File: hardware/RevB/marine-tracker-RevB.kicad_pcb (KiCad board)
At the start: 2 copper layers, 65 x 58 mm, 108 parts, among them J1 USB-C, J2 BATTERY, J3 LTE_U.FL, J4 GNSS_L1_L5_U.FL, J5 Nano_SIM, Q1 AO3401A_REVERSE_POLARITY, Q2 MMBT2222A, U1 A7670G-LABE, U10 TPS3808G09DBVR, U11 TPL5111DDCR, U12 SN74LVC2G08DCUR, U13 SN74LVC1G14DBVR, U2 LC29H-AA, U3 BQ24074RGTR, U4 TPS7A2033PDBV, U5 TXS0104EPW, U6 W25Q32JWSSIM, U7 TPS22917DBV_GNSS_LOAD, U8 TPL5010_10MIN_WATCHDOG, U9 TPS3839K33DBZR

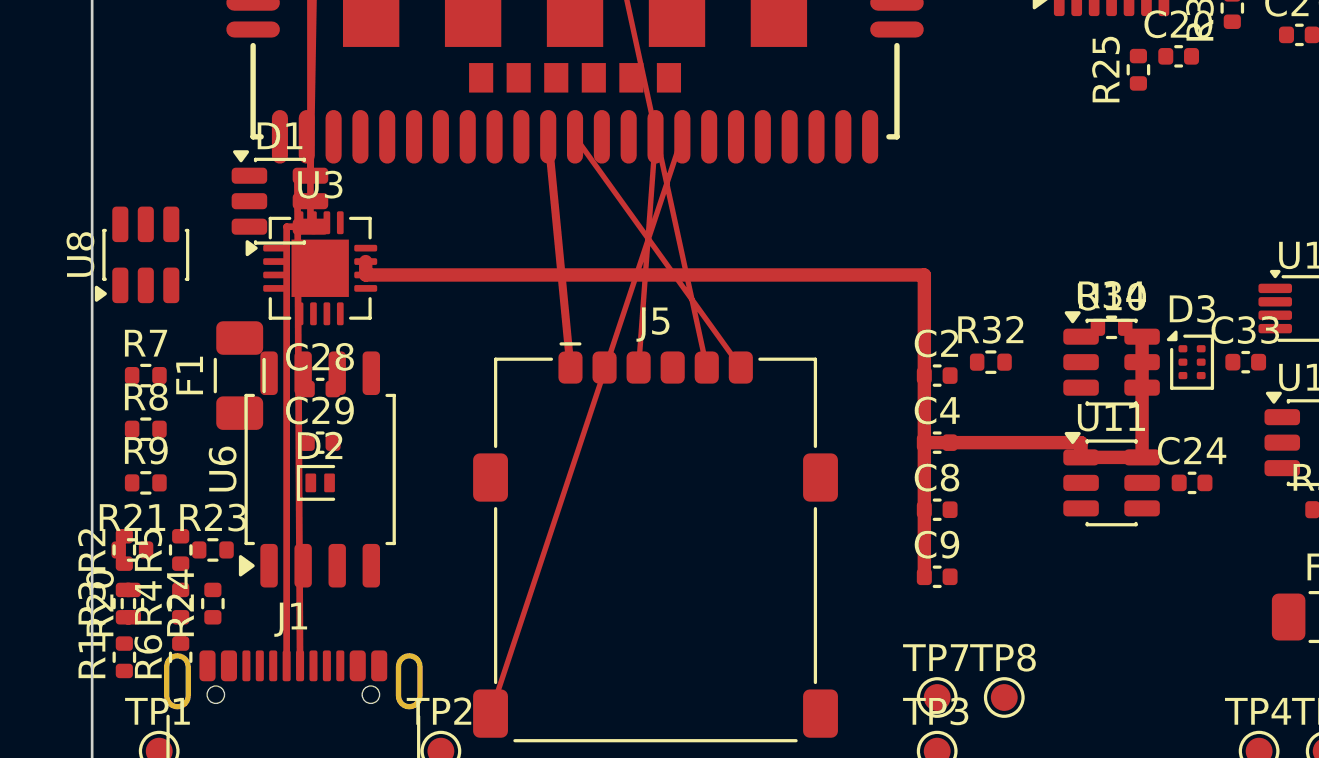
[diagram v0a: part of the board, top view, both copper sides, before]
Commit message: checkpoint: preserve RevB recovery routing state
Preserves the current validated RevB engineering checkpoint: WDT_DELAY and
WDT_RST_TRIG CONTROL routing (write-pass verified), the R21/R34 placement
correction, and the In1.Cu GND zone refill, plus documentation brought
current to RevB (STATUS.md, DESIGN_SPECIFICATION.md, VALIDATION_CHECKLIST.md).

Live-verified before commit: PCB trace/via geometry matches STATUS.md's
documented routes exactly (7 WDT_DELAY segments, 6 WDT_RST_TRIG segments,
R21/R34 pad positions), no protected net (VBAT_MODEM/VSYS/RF/USB/SIM)
geometry touched, no In1.Cu CONTROL signal routing, and DRC totals
(213 errors / 214 warnings / 427 total) unchanged from the documented
baseline.

This is a checkpoint, not a completion declaration: Recovery/Control
routing remains partially open (5 of 7 nets), and RevB is not DRC-clean.

Excludes hardware/RevB/marine-tracker-RevB_drc_violations.json (generated,
machine-path-embedded, reproducible diagnostic artifact) and .mcp.json /
.agents/ (machine-specific tool config, handled separately by the
workstation migration package).

Co-Authored-By: Claude Sonnet 5 <noreply@anthropic.com>
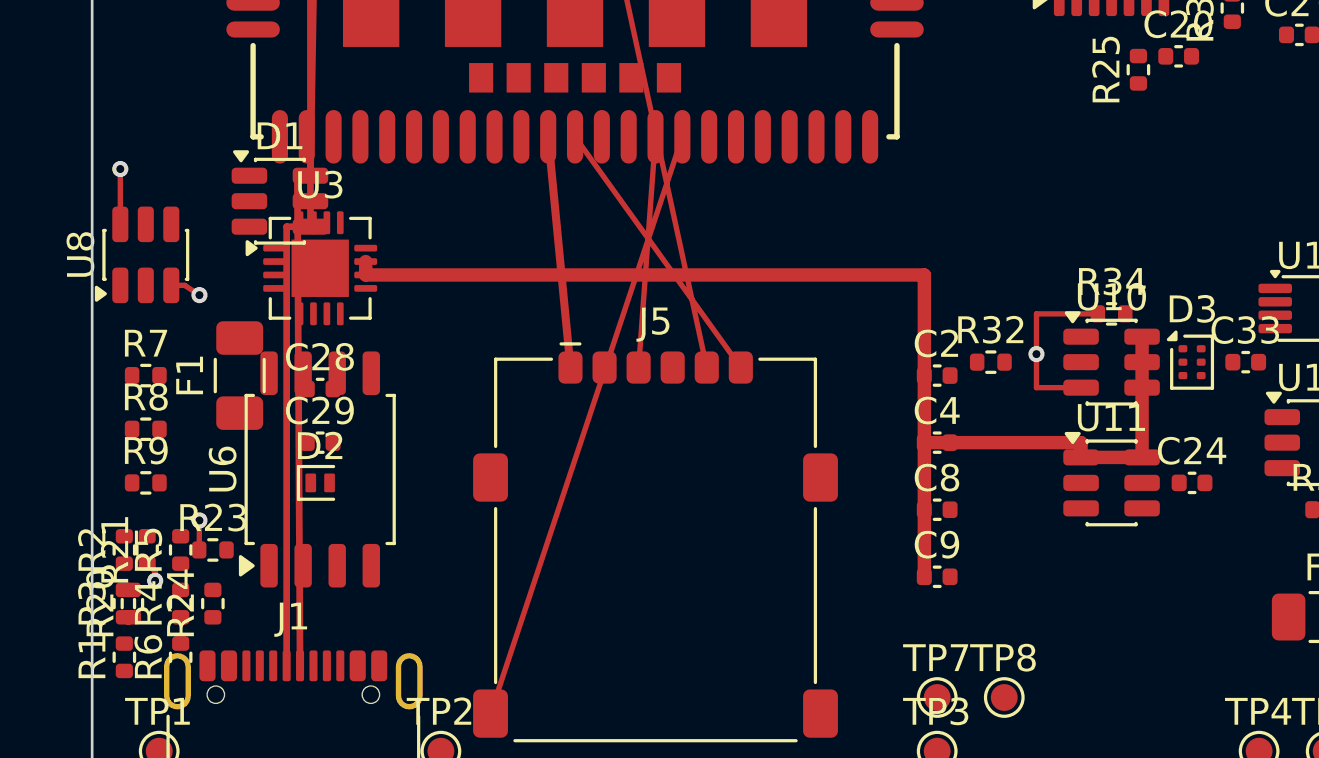
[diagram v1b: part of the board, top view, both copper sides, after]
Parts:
- moved R21 0.55 mm to (2.05, 47.5), turned to 90 degrees
- moved R34 0.50 mm to (38.0, 38.7)
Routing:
- net WDT_RST_TRIG: track 0.00 -> 43.6 mm, vias 0 -> 2
- net WDT_DELAY: track 0.00 -> 14.2 mm, vias 0 -> 3
- added copper zone on In1.Cu, net GND
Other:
- copper layers 2 -> 4
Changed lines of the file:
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@@
 	(generator_version "10.0")
 	(general
-		(thickness 1.6)
+		(thickness 1.6062)
 		(legacy_teardrops no)
 	)
@@
 	(layers
 		(0 "F.Cu" signal)
+		(4 "In1.Cu" signal)
+		(6 "In2.Cu" signal)
 		(2 "B.Cu" signal)
 		(9 "F.Adhes" user "F.Adhesive")
@@
 	)
 	(setup
+		(stackup
+			(layer "F.SilkS"
+				(type "Top Silk Screen")
+			)
+			(layer "F.Paste"
+				(type "Top Solder Paste")
+			)
+			(layer "F.Mask"
+				(type "Top Solder Mask")
+				(thickness 0.01)
+			)
+			(layer "F.Cu"
+				(type "copper")
+				(thickness 0.035)
+			)
+			(layer "dielectric 1"
+				(type "prepreg")
+				(thickness 0.2104)
+				(material "FR4")
+				(epsilon_r 4.4)
+				(loss_tangent 0.02)
+			)
+			(layer "In1.Cu"
+				(type "copper")
+				(thickness 0.0152)
+			)
+			(layer "dielectric 2"
+				(type "core")
+				(thickness 1.065)
+				(material "FR4")
+				(epsilon_r 4.6)
+				(loss_tangent 0.02)
+			)
+			(layer "In2.Cu"
+				(type "copper")
+				(thickness 0.0152)
+			)
+			(layer "dielectric 3"
+				(type "prepreg")
+				(thickness 0.2104)
+				(material "FR4")
+				(epsilon_r 4.4)
+				(loss_tangent 0.02)
+			)
+			(layer "B.Cu"
+				(type "copper")
+				(thickness 0.035)
+			)
+			(layer "B.Mask"
+				(type "Bottom Solder Mask")
+				(thickness 0.01)
+			)
+			(layer "B.Paste"
+				(type "Bottom Solder Paste")
+			)
+			(layer "B.SilkS"
+				(type "Bottom Silk Screen")
+			)
+			(copper_finish "None")
+			(dielectric_constraints no)
+		)
 		(pad_to_mask_clearance 0)
 		(allow_soldermask_bridges_in_footprints no)
@@
 		(capping no)
 		(filling no)
+		(zone_defaults)
 		(pcbplotparams
 			(layerselection 0x00000000_00000000_55555555_5755f5ff)
@@
 	(footprint "Resistor_SMD:R_0402_1005Metric"
 		(layer "F.Cu")
-		(at 38 39.2)
+		(at 38 38.7)
 		(descr "Resistor SMD 0402 (1005 Metric), square (rectangular) end terminal, IPC-7351 nominal, (Body size source: IPC-SM-782 page 72, https://www.pcb-3d.com/wordpress/wp-content/uploads/ipc-sm-782a_amendment_1_and_2.pdf)")
 		(tags "resistor")
@@
 	(footprint "Resistor_SMD:R_0402_1005Metric"
 		(layer "F.Cu")
-		(at 1.5 47.5)
+		(at 2.049999 47.5 90)
 		(descr "Resistor SMD 0402 (1005 Metric), square (rectangular) end terminal, IPC-7351 nominal, (Body size source: IPC-SM-782 page 72, https://www.pcb-3d.com/wordpress/wp-content/uploads/ipc-sm-782a_amendment_1_and_2.pdf)")
 		(tags "resistor")
 		(property "Reference" "R21"
-			(at 0 -1.17 0)
+			(at 0 -1.17 90)
 			(layer "F.SilkS")
 			(effects
@@
 		)
 		(property "Value" "124k_1%"
-			(at 0 1.17 0)
+			(at 0 1.17 90)
 			(layer "F.Fab")
 			(effects
@@
 		)
 		(property "Datasheet" ""
-			(at 0 0 0)
+			(at 0 0 90)
 			(layer "F.Fab")
 			(hide yes)
@@
 		)
 		(property "Description" ""
-			(at 0 0 0)
+			(at 0 0 90)
 			(layer "F.Fab")
 			(hide yes)
@@
 		)
 		(property "KiLib_Generator" "SMD_2terminal_chip_molded"
-			(at 0 0 0)
+			(at 0 0 90)
 			(layer "F.SilkS")
 			(hide yes)
@@
 		)
 		(fp_text user "${REFERENCE}"
-			(at 0 0 0)
+			(at 0 0 90)
 			(layer "F.Fab")
 			(effects
@@
 		)
 		(pad "1" smd roundrect
-			(at -0.51 0)
+			(at -0.51 0 90)
 			(size 0.54 0.64)
 			(layers "F.Cu" "F.Mask" "F.Paste")
@@
 		)
 		(pad "2" smd roundrect
-			(at 0.51 0)
+			(at 0.51 0 90)
 			(size 0.54 0.64)
 			(layers "F.Cu" "F.Mask" "F.Paste")
@@
 	)
 	(segment
+		(start 35.2 40.2)
+		(end 35.2 38.7)
+		(width 0.2)
+		(layer "F.Cu")
+		(net "WDT_RST_TRIG")
+	)
+	(segment
+		(start 35.2 40.2)
+		(end 35.2 41.45)
+		(width 0.2)
+		(layer "F.Cu")
+		(net "WDT_RST_TRIG")
+	)
+	(segment
+		(start 35.2 41.45)
+		(end 36.8625 41.45)
+		(width 0.2)
+		(layer "F.Cu")
+		(net "WDT_RST_TRIG")
+	)
+	(segment
+		(start 1.05 35.3625)
+		(end 1.05 33.299999)
+		(width 0.2)
+		(layer "F.Cu")
+		(net "WDT_RST_TRIG")
+	)
+	(segment
+		(start 35.2 38.7)
+		(end 37.49 38.7)
+		(width 0.2)
+		(layer "F.Cu")
+		(net "WDT_RST_TRIG")
+	)
+	(via
+		(at 35.2 40.2)
+		(size 0.6)
+		(drill 0.3)
+		(layers "F.Cu" "B.Cu")
+		(net "WDT_RST_TRIG")
+	)
+	(via
+		(at 1.05 33.299999)
+		(size 0.6)
+		(drill 0.3)
+		(layers "F.Cu" "B.Cu")
+		(net "WDT_RST_TRIG")
+	)
+	(segment
+		(start 1.05 33.299999)
+		(end 35.2 40.2)
+		(width 0.2)
+		(layer "In2.Cu")
+		(net "WDT_RST_TRIG")
+	)
+	(segment
 		(start 39.2 5.4125)
 		(end 39.2 8.715)
@@
 		(net "VBAT_MODEM")
 	)
+	(segment
+		(start 2.95 37.6375)
+		(end 3.45 37.6375)
+		(width 0.2)
+		(layer "F.Cu")
+		(net "WDT_DELAY")
+	)
+	(segment
+		(start 3.45 37.6375)
+		(end 4 38)
+		(width 0.2)
+		(layer "F.Cu")
+		(net "WDT_DELAY")
+	)
+	(segment
+		(start 3.99 47.5)
+		(end 4 46.4)
+		(width 0.2)
+		(layer "F.Cu")
+		(net "WDT_DELAY")
+	)
+	(segment
+		(start 2.049999 48.01)
+		(end 2.35 48.3)
+		(width 0.2)
+		(layer "F.Cu")
+		(net "WDT_DELAY")
+	)
+	(segment
+		(start 2.35 48.3)
+		(end 2.35 48.65)
+		(width 0.2)
+		(layer "F.Cu")
+		(net "WDT_DELAY")
+	)
+	(via
+		(at 4 46.4)
+		(size 0.6)
+		(drill 0.3)
+		(layers "F.Cu" "B.Cu")
+		(net "WDT_DELAY")
+	)
+	(via
+		(at 2.35 48.65)
+		(size 0.6)
+		(drill 0.3)
+		(layers "F.Cu" "B.Cu")
+		(net "WDT_DELAY")
+	)
+	(via
+		(at 4 38)
+		(size 0.6)
+		(drill 0.3)
+		(layers "F.Cu" "B.Cu")
+		(net "WDT_DELAY")
+	)
+	(segment
+		(start 4 38)
+		(end 4 46.4)
+		(width 0.2)
+		(layer "In2.Cu")
+		(net "WDT_DELAY")
+	)
+	(segment
+		(start 4 46.4)
+		(end 2.35 48.65)
+		(width 0.2)
+		(layer "In2.Cu")
+		(net "WDT_DELAY")
+	)
+	(zone
+		(net "GND")
+		(layer "In1.Cu")
+		(hatch edge 0.5)
+		(connect_pads
+			(clearance 0.5)
+		)
+		(min_thickness 0.25)
+		(fill yes
+			(thermal_gap 0.5)
+			(thermal_bridge_width 0.5)
+			(island_removal_mode 0)
+		)
+		(polygon
+			(pts
+				(xy 0 0) (xy 0 58) (xy 65 58) (xy 65 0)
+			)
+		)
+	)
 	(embedded_fonts no)
